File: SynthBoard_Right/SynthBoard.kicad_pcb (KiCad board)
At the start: 2 copper layers, 155 x 80 mm, 123 parts, among them IC1 AS321KTR-G1, IC2 AS321KTR-G1, IC8 PIC16F13145-I/SO, J1 DigiInput, J10 AudioOut, J2 InLFO OutEnv, J3 D_Power, J5 ICSP EG, J6 A_Power, J8 VCFOut, Q3 2SA812, Q4 2SC1623(RANGE:300-400), Q6 2SA812, Q7 2SA812, Q8 2SA812, U2 LM13700, U3 Opamp_Dual, U4 Opamp_Dual, U5 LM13700, U6 Opamp_Dual, U8 LM13700, U9 MCP6232-E_P

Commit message: SynthBoard Right
配線ミスを修正
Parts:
- removed J2: InLFO OutEnv, Connector_PinSocket_2.54mm:PinSocket_1x03_P2.54mm_Vertical
- added J4: ConnLeft, Connector_PinSocket_2.54mm:PinSocket_1x04_P2.54mm_Vertical, F.Cu at (252.5, 48.9)
- U3, U4, U6: value Opamp_Dual -> TJM4558CDT
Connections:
- C9 pad 2: Net-(VR14-CCW) -> Net-(VR14-CW)
- R70 pad 2: Net-(VR14-CCW) -> Net-(VR14-CW)
- VR14 pad 1: Net-(VR14-CCW) -> GNDA
- VR14 pad 3: GNDA -> Net-(VR14-CW)
- VR19 pad 1: +12VA -> -12VA
- VR19 pad 3: -12VA -> +12VA
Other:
- board text added: "In VCO"

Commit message: SynthBoard Right
Basic部品で更新まで
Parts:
- removed Q3: 2SA812, SamacSys_parts:SOT95P240X120-3N
- added Q1: SS8050(RANGE:200-350), Package_TO_SOT_SMD:SOT-23, F.Cu at (264.5, 95.4)
- C10, C11, C4, C8: value 0805B221K500NT -> ECH-U1H221JX5
- C15, C21, C22: value 0805B103J500NT -> CL21B103KBANNNC
- Q4: value 2SC1623(RANGE:300-400) -> 2SA812; footprint SamacSys_parts:SOT95P237X125-3N -> SamacSys_parts:SOT95P240X120-3N
- R1, R2, R3, R31, R32, R50, R52, R57, R66, R70, R74: value 0805W8J0104T5E -> 0805W8F1003T5E
- R64, R77, R86: value 0805W8J0512T5E -> 0805W8F5101T5E
- U3, U4, U6: value TJM4558CDT -> TL072CDT
- moved R86 5.58 mm to (214.4, 48.1), turned to 0 degrees
- moved Q8 5.51 mm to (210.2, 49.0)
- moved R50 4.26 mm to (262.9, 91.9), turned to 0 degrees
- moved Q4 3.48 mm to (260.3, 95.1)
- moved R49 3.08 mm to (256.9, 93.2)
- moved R76 2.08 mm to (195.6, 51.9), turned to 180 degrees
- moved R67 1.86 mm to (256.3, 116.8)
- moved R74 1.69 mm to (195.6, 54.6), turned to 0 degrees
- moved R66 1.67 mm to (256.3, 110.5), turned to 0 degrees
- moved R51 1.49 mm to (256.9, 98.5)
- moved C7 1.42 mm to (256.3, 112.5), turned to 180 degrees
- moved R28 1.22 mm to (211.1, 111.4)
- moved R60 0.97 mm to (259.0, 53.5)
- moved R57 0.97 mm to (259.0, 57.6)
- moved R46 0.80 mm to (255.9, 88.6)
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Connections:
- Q4 pad 1: Net-(Q4-B) -> Net-(Q1-E)
- Q4 pad 2: Net-(Q3-B) -> GNDA
- Q4 pad 3: +12VA -> Net-(Q4-C)
- R47 pad 2: Net-(Q4-B) -> Net-(Q1-B)
- R48 pad 2: Net-(Q4-B) -> Net-(Q1-B)
- R49 pad 2: Net-(Q4-B) -> Net-(Q1-B)
- R50 pad 2: Net-(Q3-B) -> Net-(Q1-E)
- R51 pad 1: Net-(Q3-C) -> Net-(Q4-C)
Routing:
- net -12VA: track 0.00 -> 270.5 mm, vias 0 -> 7
- net +12VA: track 0.00 -> 237.8 mm, vias 0 -> 10
- net +5VD: track 0.00 -> 185.0 mm, vias 0 -> 2
- net EnvFlt: track 0.00 -> 115.0 mm, vias 0 -> 3
- net VCOWave: track 0.00 -> 114.3 mm, vias 0 -> 1
- net GNDD: track 0.00 -> 107.1 mm, vias 0 -> 6
- net Net-(IC1-INPUT_-): track 0.00 -> 99.6 mm, vias 0 -> 1
- net VCF_OUT: track 0.00 -> 89.1 mm, vias 0 -> 3
- net VCACnt: track 0.00 -> 85.2 mm, vias 0 -> 2
- net VCFCnt: track 0.00 -> 82.0 mm
- net ResoCnt: track 0.00 -> 79.0 mm, vias 0 -> 2
- net LP12db: track 0.00 -> 64.2 mm, vias 0 -> 2
- net VCF_ResoWav: track 0.00 -> 62.4 mm, vias 0 -> 3
- net AmpWave: track 0.00 -> 51.1 mm, vias 0 -> 1
- net ~MCLR_EG: track 0.00 -> 47.7 mm, vias 0 -> 1
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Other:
- board text added: "MC2 SynthBoard Right 2025/9/21"

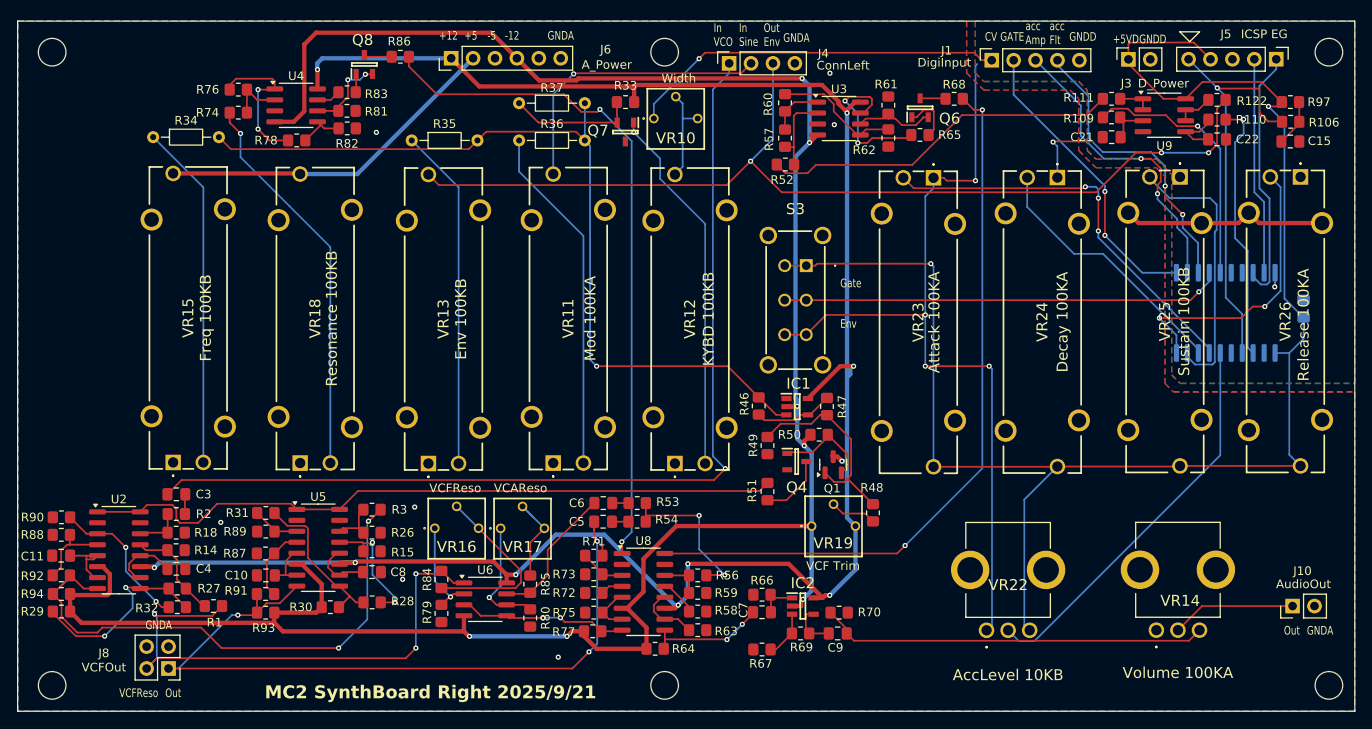
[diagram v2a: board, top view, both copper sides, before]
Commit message: MC2
まとめて登録
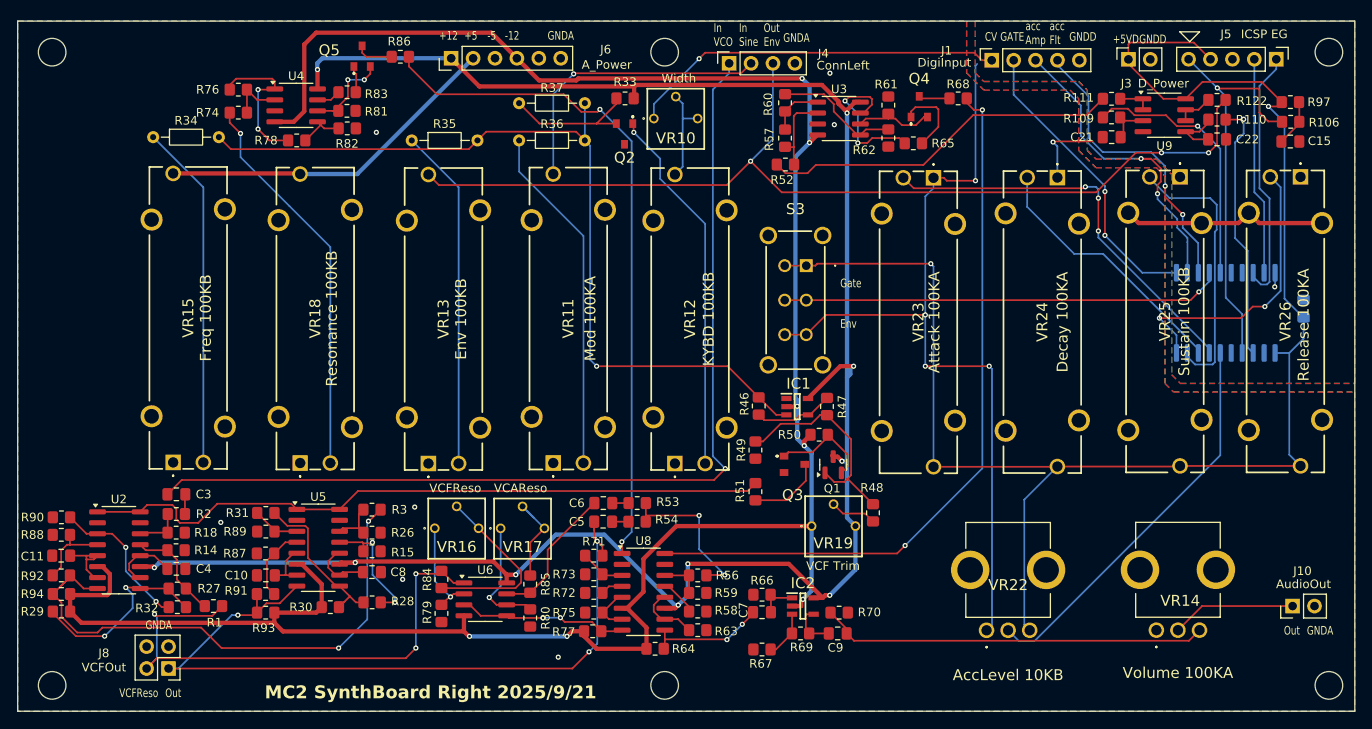
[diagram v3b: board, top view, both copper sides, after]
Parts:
- removed Q6, Q7, Q8: 2SA812, SamacSys_parts:SOT95P240X120-3N
- added Q2: 2SA1162-GR_F_, SamacSys_parts:1SS294LFT, F.Cu at (240.3, 57.1)
- added Q3: 2SA1162-GR_F_, SamacSys_parts:1SS294LFT, F.Cu at (260.0, 95.4)
- added Q5: 2SA1162-GR_F_, SamacSys_parts:1SS294LFT, F.Cu at (209.9, 48.1)
- Q4: value 2SA812 -> 2SA1162-GR_F_; footprint SamacSys_parts:SOT95P240X120-3N -> SamacSys_parts:1SS294LFT
- moved Q4 43.5 mm to (274.5, 53.9)
- moved R49 1.49 mm to (255.5, 93.7)
- moved R51 1.40 mm to (255.5, 98.6)
- moved R65 1.24 mm to (273.8, 58.2)
- moved R68 0.46 mm to (279.0, 53.0)
- moved R33 0.43 mm to (240.4, 53.0)
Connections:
- Q4 pad 1: Net-(Q1-E) -> Net-(Q4-B)
- Q4 pad 2: GNDA -> Net-(Q4-E)
- R51 pad 1: Net-(Q4-C) -> Net-(Q3-C)
- R61 pad 2: Net-(Q6-E) -> Net-(Q4-E)
- R65 pad 2: Net-(Q6-B) -> Net-(Q4-B)
- R68 pad 1: Net-(Q6-C) -> Net-(Q4-C)
- U3 pad 6: Net-(Q6-E) -> Net-(Q4-E)
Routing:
- net Net-(Q6-E): track 9.43 -> 0.00 mm
- net Net-(Q4-E): track 0.00 -> 9.30 mm
- net Net-(Q3-C): track 0.00 -> 9.02 mm
- net Net-(Q4-B): track 0.00 -> 8.85 mm
- net Net-(Q6-B): track 6.02 -> 0.00 mm
- net Net-(Q4-C): track 7.62 -> 2.98 mm
- net Net-(Q6-C): track 2.98 -> 0.00 mm
- net Net-(Q1-B): track 24.0 -> 25.6 mm
- net Net-(Q2-E): track 14.7 -> 16.1 mm
- net VCFCnt: track 82.0 -> 80.6 mm
- net Net-(Q5-C): track 3.26 -> 4.43 mm
- net Net-(Q5-B): track 2.14 -> 3.10 mm
- net Net-(R65-Pad1): track 17.9 -> 17.2 mm
- net Net-(Q5-E): track 9.99 -> 10.6 mm
